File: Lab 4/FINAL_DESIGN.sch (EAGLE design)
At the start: 21 parts, among them IC3 MAX660CPA, J1 FTDI_DEVICERA_SMT, M1 WIRELESS-NRF24L01, U2 GY-521MPU6050

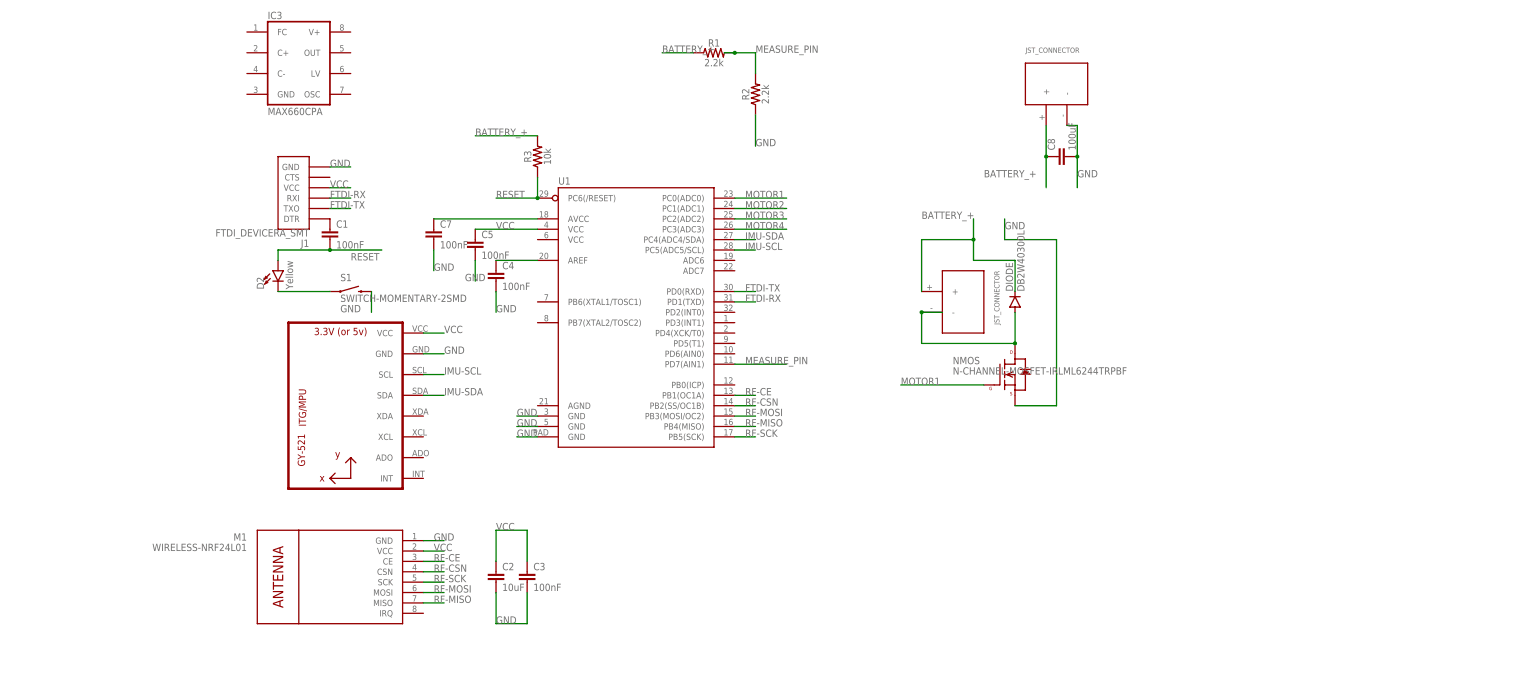
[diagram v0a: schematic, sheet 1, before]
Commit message: Added pull-down resistor; need VR connections
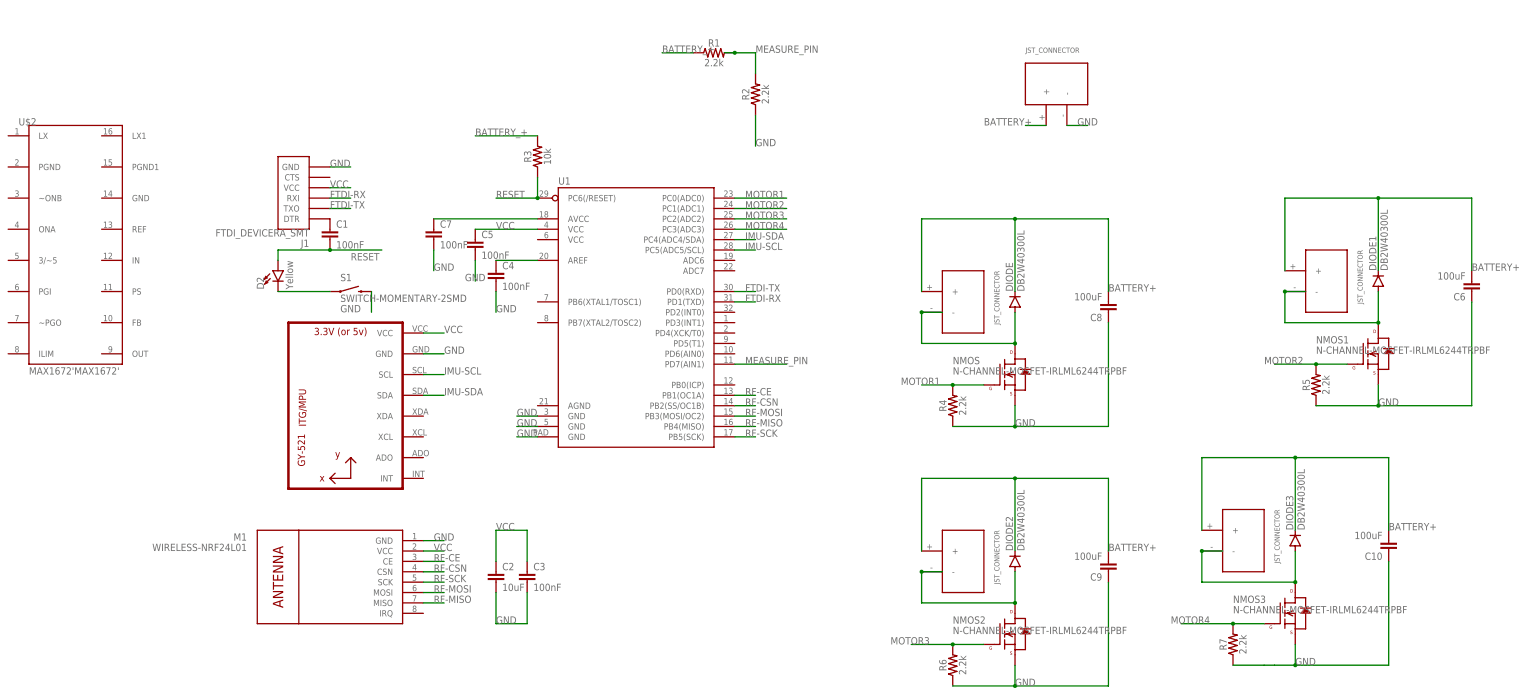
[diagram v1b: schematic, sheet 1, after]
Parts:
- removed IC3: MAX660CPA, maxim:MAX660CPA
- added C10, C6, C9: 100uF, SparkFun-Passives:CAP0603-CAP
- added DIODE1, DIODE2, DIODE3: DB2W40300L, quad:DB2W40300L
- added MOTOR1, MOTOR2, MOTOR3: JST_CONNECTOR_FEMALE, quad:JST_CONNECTOR_FEMALE
- added NMOS1, NMOS2, NMOS3: N-CHANNEL-MOSFET-IRLML6244TRPBF, quad:N-CHANNEL-MOSFET-IRLML6244TRPBF
- added R4, R5, R6, R7: 2.2k, SparkFun-Resistors:2.2KOHM-0603-1/10W-1%
- added U$2: MAX1672'MAX1672', voltreg:MAX1672'MAX1672'
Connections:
- new net BATTERY+: C10.2, C6.2, C8.2, C9.2, DIODE.GPIN, DIODE1.GPIN, DIODE2.GPIN, DIODE3.GPIN, MOTOR.+, MOTOR1.+, MOTOR2.+, MOTOR3.+, U$1.+
- new net N$4: DIODE1.PPIN, MOTOR1.-, NMOS1.D
- new net N$5: DIODE2.PPIN, MOTOR2.-, NMOS2.D
- new net N$7: DIODE3.PPIN, MOTOR3.-, NMOS3.D
- net BATTERY_+: no longer C8.1, DIODE.GPIN, MOTOR.+, U$1.+
- net GND: now also C10.1, C6.1, C8.1, C9.1, NMOS1.S, NMOS2.S, NMOS3.S, R4.1, R5.1, R6.1, R7.1; no longer C8.2
- net MOTOR1: now also R4.2
- net MOTOR2: now also NMOS1.G, R5.2
- net MOTOR3: now also NMOS2.G, R6.2
- net MOTOR4: now also NMOS3.G, R7.2
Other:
- moved on the sheet: C8

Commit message: Need oscillator, leds
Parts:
- added C11, C12, C13, C14: 100nF, SparkFun-Passives:CAP0603-CAP
- added DIODE4: DB2W40300L, quad:DB2W40300L
- added L1: 33nH/±5%/500mA, SparkFun-Coils:INDUCTOR-0603-33NH
- added R10, R11, R12, R8, R9: 10k, SparkFun-Resistors:2.2KOHM-0603-1/10W-1%
- R4, R5, R6, R7: value 2.2k -> 10k
- U1: value (none) -> 3.3V
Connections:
- removed net BATTERY_+: R1.1, R3.2
- new net VR-FB: R8.1, R9.2, U$2.FB
- new net VR-IN: C12.1, L1.1, R10.2, U$2.IN
- new net VR-LX: DIODE4.PPIN, L1.2, U$2.LX
- new net VR-OUT: C14.1, R12.2, R8.2, U$2.OUT
- new net VR-PGI: R10.1, R11.2, U$2.PGI
- new net VR-PS: C13.1, DIODE4.GPIN, U$2.PS
- new net VR-REF: C11.1, U$2.REF
- new net VR-~PGO: R12.1, U$2.~PGO
- net BATTERY+: now also R1.1
- net GND: now also C11.2, C12.2, C13.2, C14.2, R11.1, R9.1, U$2.3/~5, U$2.GND, U$2.PGND
- net VCC: now also R3.2
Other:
- moved on the sheet: U$2
